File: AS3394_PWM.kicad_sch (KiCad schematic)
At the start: 87 parts, among them U4 LM324, U5 AS3394, U6 LM324

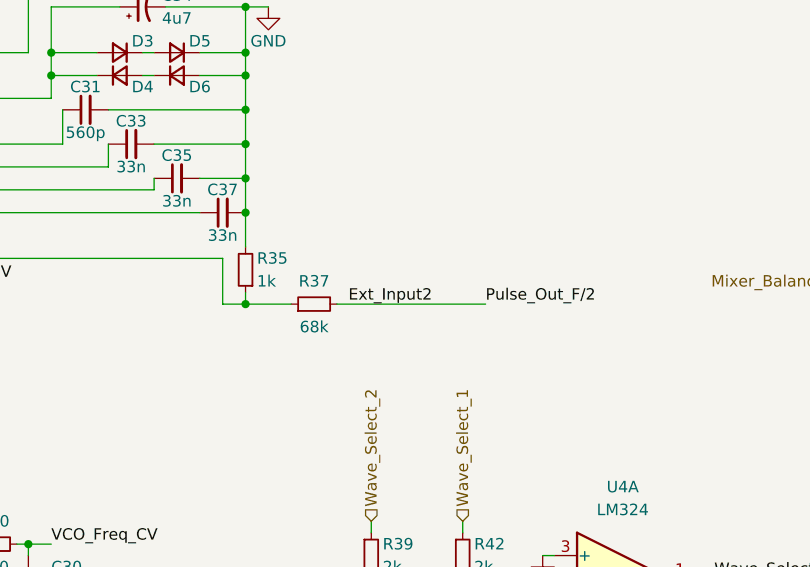
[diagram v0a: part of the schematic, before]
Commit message: Updated to Kicad 7
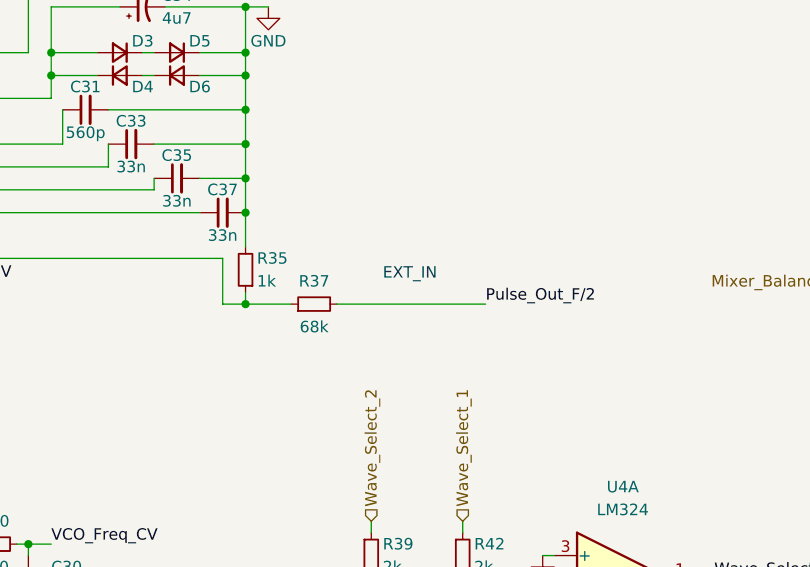
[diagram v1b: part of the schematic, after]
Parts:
- U5: symbol Bushwhacker:AS3394 -> bushwhacker:AS3394
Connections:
- net Ext_Input2 renamed Pulse_Out_F/2
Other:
- note added: "EXT_IN"

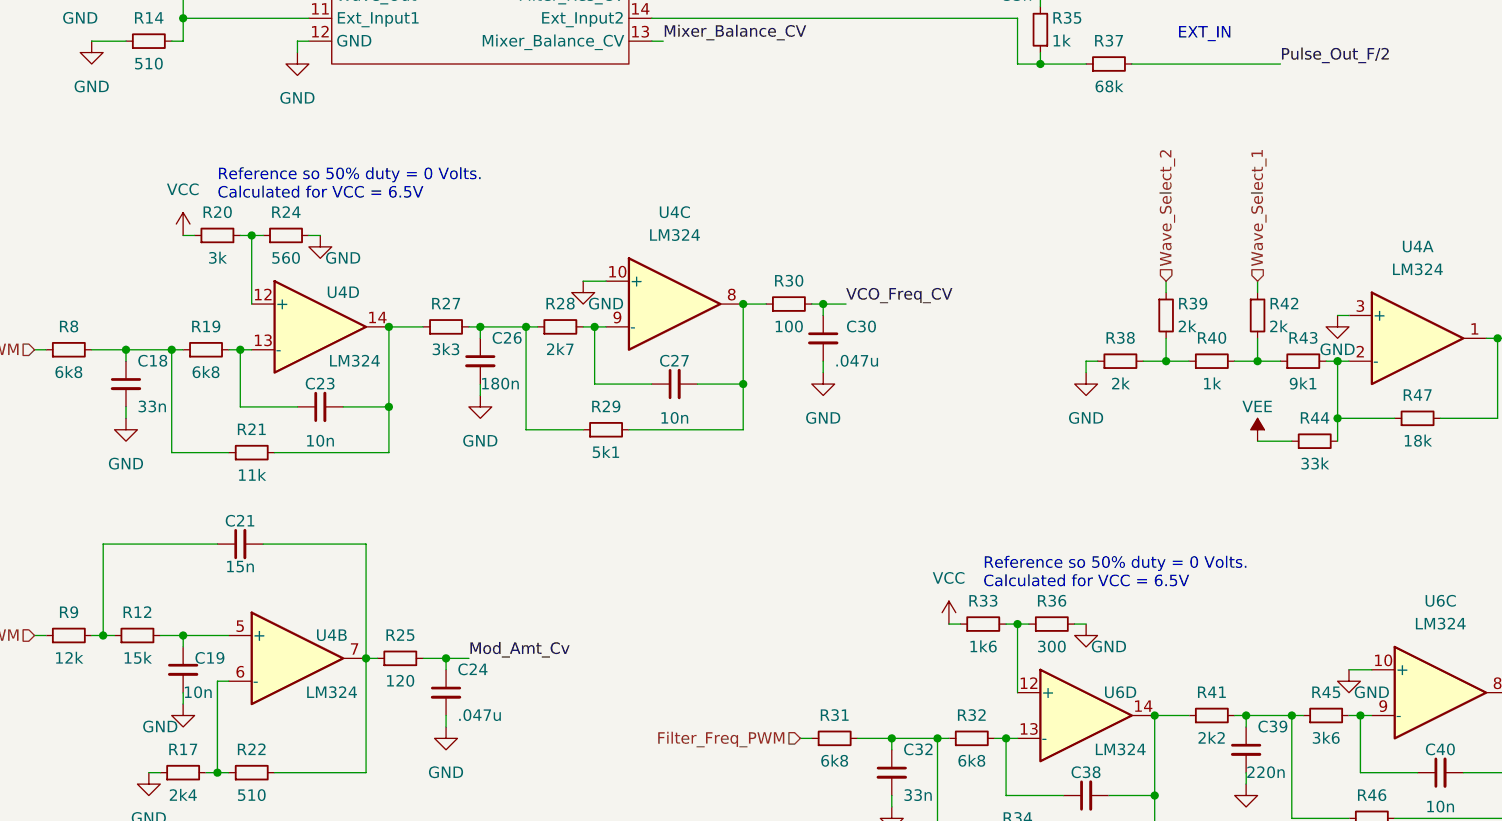
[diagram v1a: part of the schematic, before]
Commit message: Reworked op-amp bias to use 5V LDO reference instead of 6.5V vin
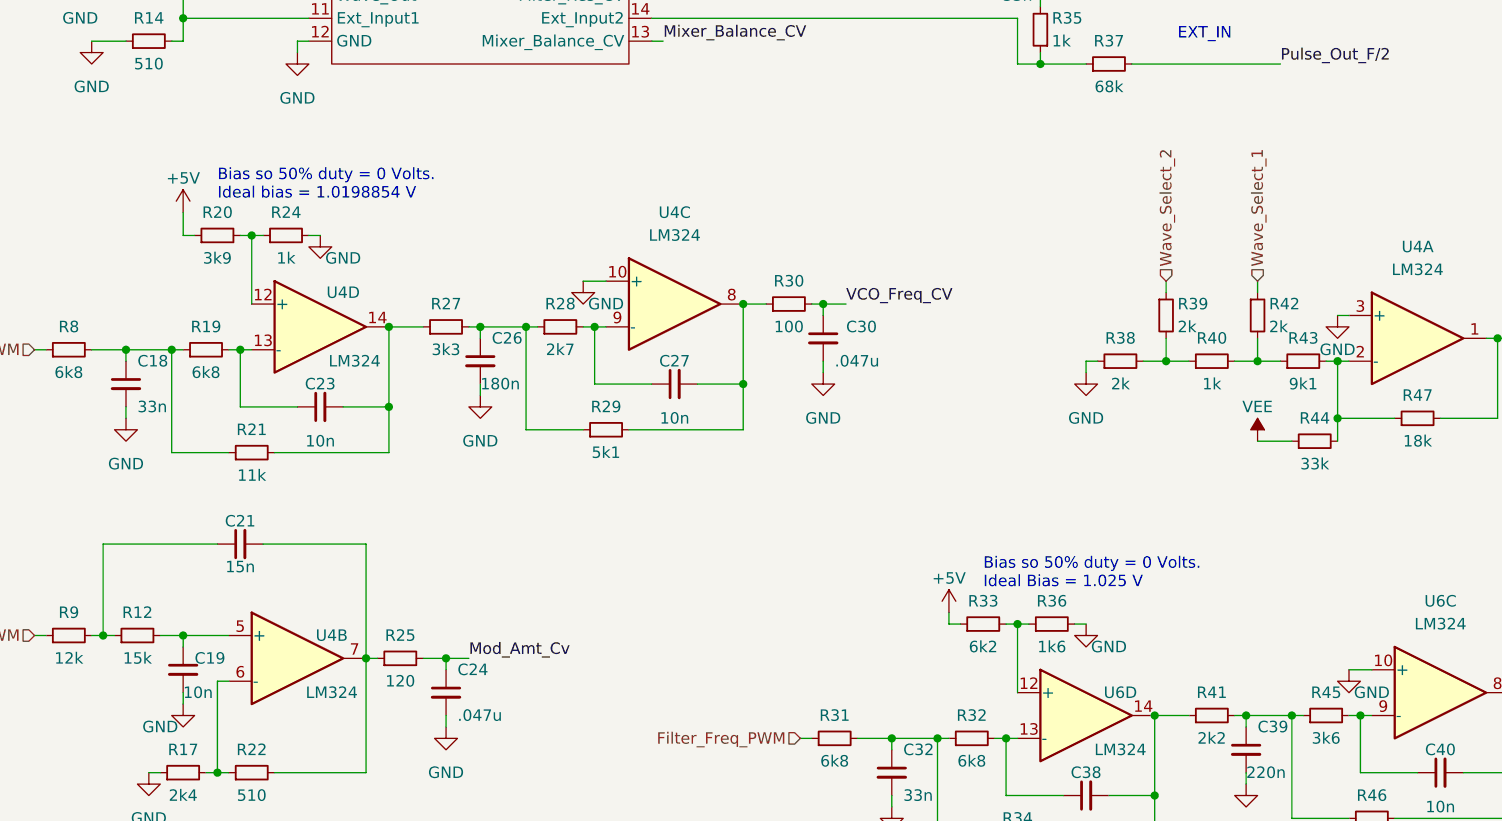
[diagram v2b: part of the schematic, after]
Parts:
- R20: value 3k -> 3k9; footprint Resistor_SMD:R_0603_1608Metric -> Resistor_SMD:R_0402_1005Metric
- R24: value 560 -> 1k; footprint Resistor_SMD:R_0603_1608Metric -> Resistor_SMD:R_0402_1005Metric
- R33: value 1k6 -> 6k2; footprint Resistor_SMD:R_0402_1005Metric -> Resistor_SMD:R_0603_1608Metric
- R36: value 300 -> 1k6
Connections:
- net +5V: now also R20.1, R33.1
- net VCC: no longer R20.1, R33.1
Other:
- note added: "Bias so 50% duty = 0 Volts. Ideal Bias = 1.025 V"
- note added: "Bias so 50% duty = 0 Volts. Ideal bias = 1.0198854 V"
- note removed: "Reference so 50% duty = 0 Volts. Calculated for VCC = 6.5V"
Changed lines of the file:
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@@
+    (stroke (width 0) (type default))
+  )
+  (wire (pts (xy 48.26 92.71) (xy 48.26 95.25))
     (stroke (width 0) (type default))
   )
@@
     (stroke (width 0) (type default))
   )
+  (wire (pts (xy 133.35 137.16) (xy 133.35 138.43))
+    (stroke (width 0) (type default))
+  )
   (wire (pts (xy 195.58 146.05) (xy 198.12 146.05))
     (stroke (width 0) (type default))
@@
     (stroke (width 0) (type default))
   )
-  (text "Reference so 50% duty = 0 Volts. \nCalculated for VCC = 6.5V"
-    (at 137.16 134.62 0)
+  (text "Bias so 50% duty = 0 Volts. \nIdeal Bias = 1.025 V" (at 137.16 134.62 0)
     (effects (font (size 1.27 1.27)) (justify left bottom))
   )
@@
     (effects (font (size 1.27 1.27)) (justify left bottom))
   )
-  (text "Reference so 50% duty = 0 Volts. \nCalculated for VCC = 6.5V"
+  (text "Bias so 50% duty = 0 Volts. \nIdeal bias = 1.0198854 V"
     (at 52.07 91.44 0)
     (effects (font (size 1.27 1.27)) (justify left bottom))
@@
         (path "/b11f2c7b-7c1a-4248-8cee-cb6fdfa459af/4be0f50f-df7d-4a82-b90c-e414038b561e"
           (reference "R23") (unit 1)
-        )
-      )
-    )
-  )
-  (symbol (lib_id "power:VCC") (at 48.26 95.25 0) (unit 1)
-    (in_bom yes) (on_board yes) (dnp no) (fields_autoplaced)
-    (property "Reference" "#PWR032" (at 48.26 99.06 0)
-      (effects (font (size 1.27 1.27)) hide)
-    )
-    (property "Value" "VCC" (at 48.26 90.17 0)
-      (effects (font (size 1.27 1.27)))
-    )
-    (property "Footprint" "" (at 48.26 95.25 0)
-      (effects (font (size 1.27 1.27)) hide)
-    )
-    (property "Datasheet" "" (at 48.26 95.25 0)
-      (effects (font (size 1.27 1.27)) hide)
-    )
-    (pin "1")
-    (instances
-      (project "RP2040_AS3394"
-        (path "/b11f2c7b-7c1a-4248-8cee-cb6fdfa459af/4be0f50f-df7d-4a82-b90c-e414038b561e"
-          (reference "#PWR032") (unit 1)
         )
       )
@@
       (effects (font (size 1.27 1.27)))
     )
-    (property "Value" "560" (at 59.69 97.79 90)
-      (effects (font (size 1.27 1.27)))
-    )
-    (property "Footprint" "Resistor_SMD:R_0603_1608Metric" (at 59.69 95.25 0)
+    (property "Value" "1k" (at 59.69 97.79 90)
+      (effects (font (size 1.27 1.27)))
+    )
+    (property "Footprint" "Resistor_SMD:R_0402_1005Metric" (at 59.69 95.25 0)
       (effects (font (size 1.27 1.27)) hide)
     )
@@
         (path "/b11f2c7b-7c1a-4248-8cee-cb6fdfa459af/4be0f50f-df7d-4a82-b90c-e414038b561e"
           (reference "R24") (unit 1)
+        )
+      )
+    )
+  )
+  (symbol (lib_id "power:+5V") (at 133.35 137.16 0) (unit 1)
+    (in_bom yes) (on_board yes) (dnp no) (fields_autoplaced)
+    (property "Reference" "#PWR032" (at 133.35 140.97 0)
+      (effects (font (size 1.27 1.27)) hide)
+    )
+    (property "Value" "+5V" (at 133.35 133.35 0)
+      (effects (font (size 1.27 1.27)))
+    )
+    (property "Footprint" "" (at 133.35 137.16 0)
+      (effects (font (size 1.27 1.27)) hide)
+    )
+    (property "Datasheet" "" (at 133.35 137.16 0)
+      (effects (font (size 1.27 1.27)) hide)
+    )
+    (pin "1")
+    (instances
+      (project "RP2040_AS3394"
+        (path "/b11f2c7b-7c1a-4248-8cee-cb6fdfa459af/4be0f50f-df7d-4a82-b90c-e414038b561e"
+          (reference "#PWR032") (unit 1)
         )
       )
@@
       (effects (font (size 1.27 1.27)))
     )
-    (property "Value" "1k6" (at 137.16 140.97 90)
-      (effects (font (size 1.27 1.27)))
-    )
-    (property "Footprint" "Resistor_SMD:R_0402_1005Metric" (at 137.16 138.43 0)
+    (property "Value" "6k2" (at 137.16 140.97 90)
+      (effects (font (size 1.27 1.27)))
+    )
+    (property "Footprint" "Resistor_SMD:R_0603_1608Metric" (at 137.16 138.43 0)
       (effects (font (size 1.27 1.27)) hide)
     )
@@
       (effects (font (size 1.27 1.27)))
     )
-    (property "Value" "3k" (at 52.07 97.79 90)
-      (effects (font (size 1.27 1.27)))
-    )
-    (property "Footprint" "Resistor_SMD:R_0603_1608Metric" (at 52.07 95.25 0)
+    (property "Value" "3k9" (at 52.07 97.79 90)
+      (effects (font (size 1.27 1.27)))
+    )
+    (property "Footprint" "Resistor_SMD:R_0402_1005Metric" (at 52.07 95.25 0)
       (effects (font (size 1.27 1.27)) hide)
     )
@@
       (effects (font (size 1.27 1.27)))
     )
-    (property "Value" "300" (at 144.78 140.97 90)
+    (property "Value" "1k6" (at 144.78 140.97 90)
       (effects (font (size 1.27 1.27)))
     )
@@
     )
   )
-  (symbol (lib_id "power:VCC") (at 133.35 138.43 0) (unit 1)
-    (in_bom yes) (on_board yes) (dnp no) (fields_autoplaced)
-    (property "Reference" "#PWR044" (at 133.35 142.24 0)
-      (effects (font (size 1.27 1.27)) hide)
-    )
-    (property "Value" "VCC" (at 133.35 133.35 0)
-      (effects (font (size 1.27 1.27)))
-    )
-    (property "Footprint" "" (at 133.35 138.43 0)
-      (effects (font (size 1.27 1.27)) hide)
-    )
-    (property "Datasheet" "" (at 133.35 138.43 0)
-      (effects (font (size 1.27 1.27)) hide)
-    )
-    (pin "1")
-    (instances
-      (project "RP2040_AS3394"
-        (path "/b11f2c7b-7c1a-4248-8cee-cb6fdfa459af/4be0f50f-df7d-4a82-b90c-e414038b561e"
-          (reference "#PWR044") (unit 1)
-        )
-      )
-    )
-  )
   (symbol (lib_id "power:GND") (at 246.38 35.56 0) (unit 1)
     (in_bom yes) (on_board yes) (dnp no) (fields_autoplaced)
@@
         )
       )
+    )
+  )
+  (symbol (lib_id "power:+5V") (at 48.26 92.71 0) (unit 1)
+    (in_bom yes) (on_board yes) (dnp no) (fields_autoplaced)
+    (property "Reference" "#PWR017" (at 48.26 96.52 0)
+      (effects (font (size 1.27 1.27)) hide)
+    )
+    (property "Value" "+5V" (at 48.26 88.9 0)
+      (effects (font (size 1.27 1.27)))
+    )
+    (property "Footprint" "" (at 48.26 92.71 0)
+      (effects (font (size 1.27 1.27)) hide)
+    )
+    (property "Datasheet" "" (at 48.26 92.71 0)
+      (effects (font (size 1.27 1.27)) hide)
+    )
+    (pin "1")
+    (instances
+      (project "RP2040_AS3394"
+        (path "/b11f2c7b-7c1a-4248-8cee-cb6fdfa459af/4be0f50f-df7d-4a82-b90c-e414038b561e"
+          (reference "#PWR017") (unit 1)
+        )
+      )
